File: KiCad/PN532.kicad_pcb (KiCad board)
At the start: 2 copper layers, 42 x 42 mm, 50 parts, among them J1 Bell, J2 Header, J3 SPOX, J4 MiniGrid, SW1 TAMPER, U1 PN532, U2 QR, Y1 27.12MHz

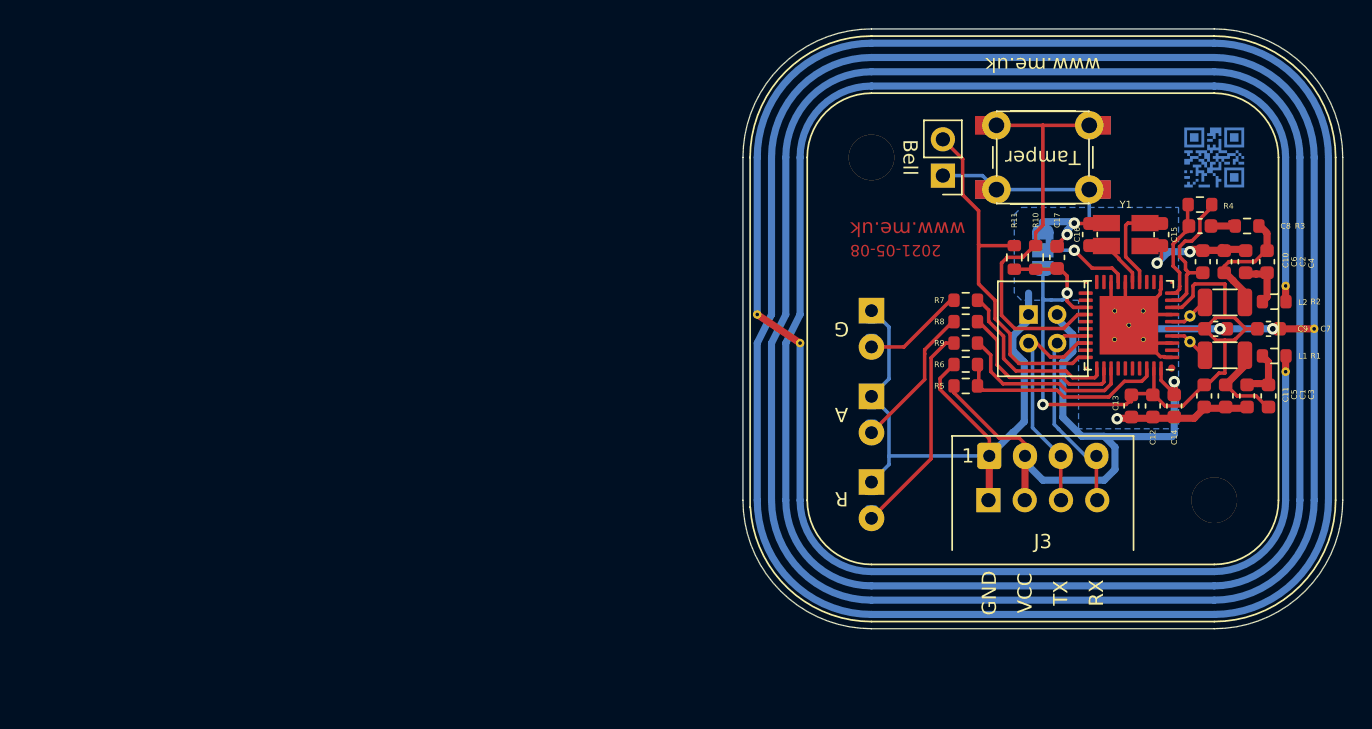
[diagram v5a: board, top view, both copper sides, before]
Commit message: Complete re-layout (needs 3D case changes still)
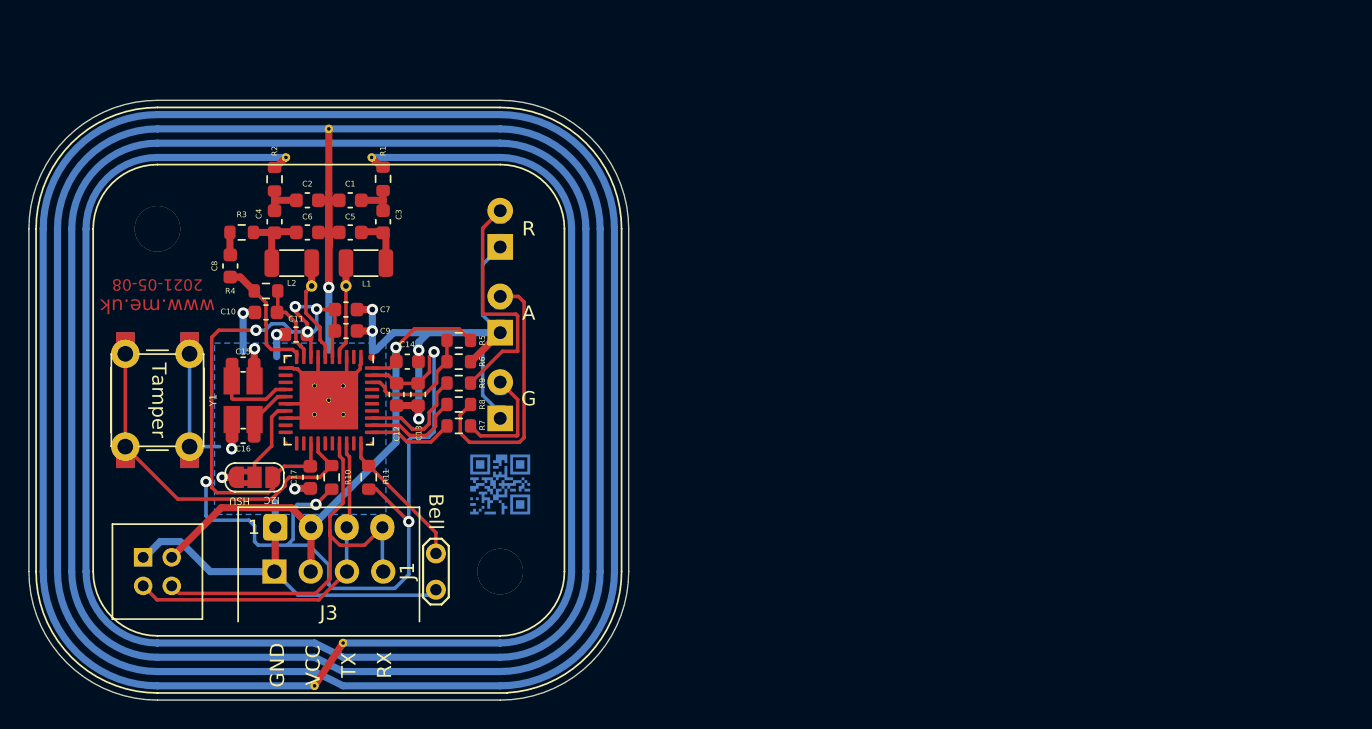
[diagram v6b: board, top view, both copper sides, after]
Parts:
- removed ? (x2): , 
- J1: footprint Connector_PinHeader_2.54mm:PinHeader_1x02_P2.54mm_Vertical -> TestPoint:TestPoint_2Pads_Pitch2.54mm_Drill0.8mm
- JP1: moved to F.Cu
- moved R2 70.5 mm to (96.2, 84.5), turned to 90 degrees
- moved R3 70.4 mm to (93.9, 88.2)
- moved C4 69.6 mm to (96.2, 87.5), turned to 270 degrees
- moved C8 68.0 mm to (93.1, 90.6), turned to 90 degrees
- moved C2 65.8 mm to (98.5, 86.0), turned to 180 degrees
- moved C10 65.7 mm to (95.6, 93.8), turned to 180 degrees
- moved R4 65.7 mm to (95.6, 92.3)
- moved L2 65.4 mm to (97.4, 90.4), turned to 0 degrees
- moved C15 64.9 mm to (94.0, 97.5), turned to 0 degrees
- moved C7 64.6 mm to (101.2, 93.7)
- moved J4 64.3 mm to (88.0, 112.0)
- moved SW1 64.3 mm to (88.0, 100.0), turned to 270 degrees
- moved C1 64.3 mm to (101.5, 86.0), turned to 180 degrees
- moved C6 64.2 mm to (98.5, 88.2), turned to 180 degrees
- moved C11 63.7 mm to (97.7, 95.4), turned to 180 degrees
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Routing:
- net +3V3: track 55.5 -> 94.4 mm, vias 2 -> 8
- net Net-(J1-Pad2): track 25.3 -> 9.88 mm
- net Net-(J2-Pad4): track 15.0 -> 29.6 mm
- net Net-(D2-Pad2): track 10.1 -> 18.5 mm
- net Net-(J2-Pad3): track 16.7 -> 24.6 mm
- net Net-(R5-Pad1): track 15.3 -> 8.63 mm
- net Net-(R7-Pad1): track 12.4 -> 6.00 mm
- net +5V: track 44.9 -> 38.9 mm
- net Net-(R8-Pad1): track 12.6 -> 6.88 mm
- net Net-(L2-Pad2): track 3.21 -> 8.00 mm
- net Net-(R9-Pad1): track 12.6 -> 7.84 mm
- net Net-(C10-Pad1): track 10.1 -> 5.78 mm
- net Net-(L1-Pad1): track 3.16 -> 7.46 mm
- net Net-(C4-Pad2): track 8.59 -> 5.18 mm
- net Net-(R10-Pad2): track 28.4 -> 25.6 mm
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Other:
- board text removed: "P30"

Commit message: Tidy
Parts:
- moved AJK1 1.50 mm to (91.9, 92.3), turned to 180 degrees
- moved C17 0.61 mm to (98.2, 105.0)
- moved R10 0.61 mm to (99.7, 105.0)
- moved R11 0.49 mm to (102.5, 105.0)
- moved C11 0.38 mm to (98.1, 95.3)
- moved C7 0.20 mm to (101.2, 93.8)
- moved C9 0.20 mm to (101.2, 95.3)
- moved U2 0.10 mm to (112.0, 106.0), turned to 180 degrees
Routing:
- net +3V3: track 94.4 -> 77.4 mm, vias 8 -> 6
- net +5V: track 38.9 -> 42.6 mm
- net Net-(R10-Pad2): track 25.6 -> 27.1 mm
- net GND: track 127.7 -> 127.2 mm

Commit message: Tweak
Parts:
- moved C7 1.50 mm to (101.2, 95.3)
- moved C9 1.50 mm to (101.2, 93.8)
